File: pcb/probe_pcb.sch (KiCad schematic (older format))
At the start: 19 parts

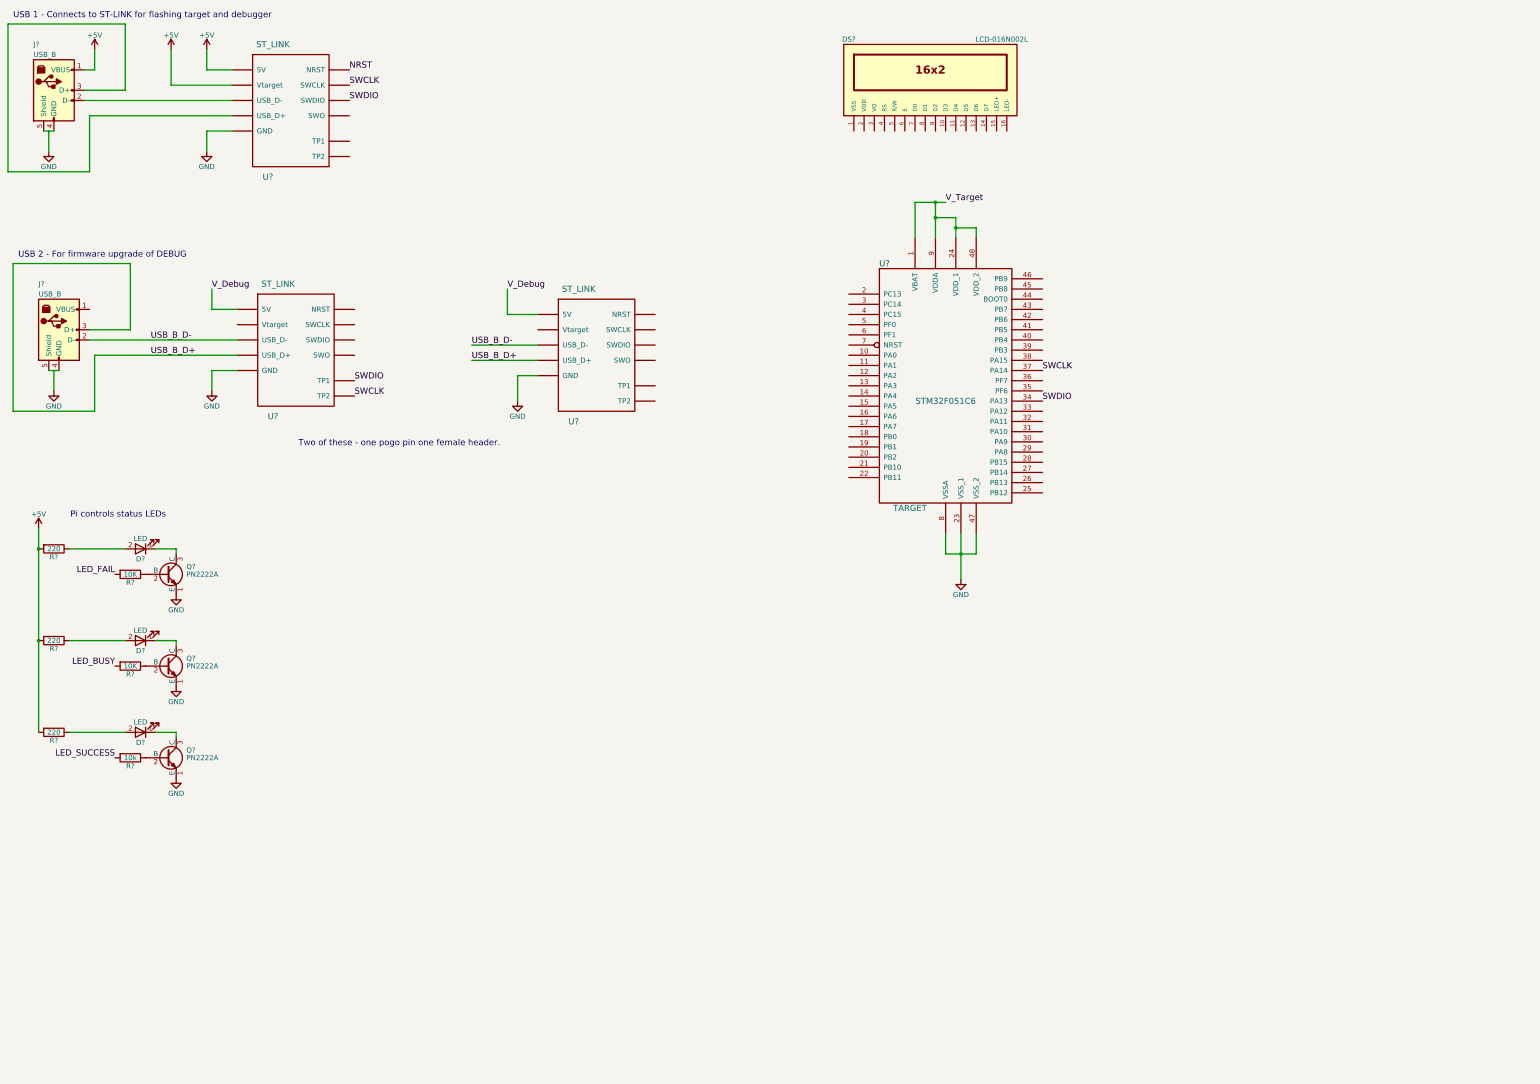
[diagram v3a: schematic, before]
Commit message: Added rough circuit for switching V_Target and V_Debug
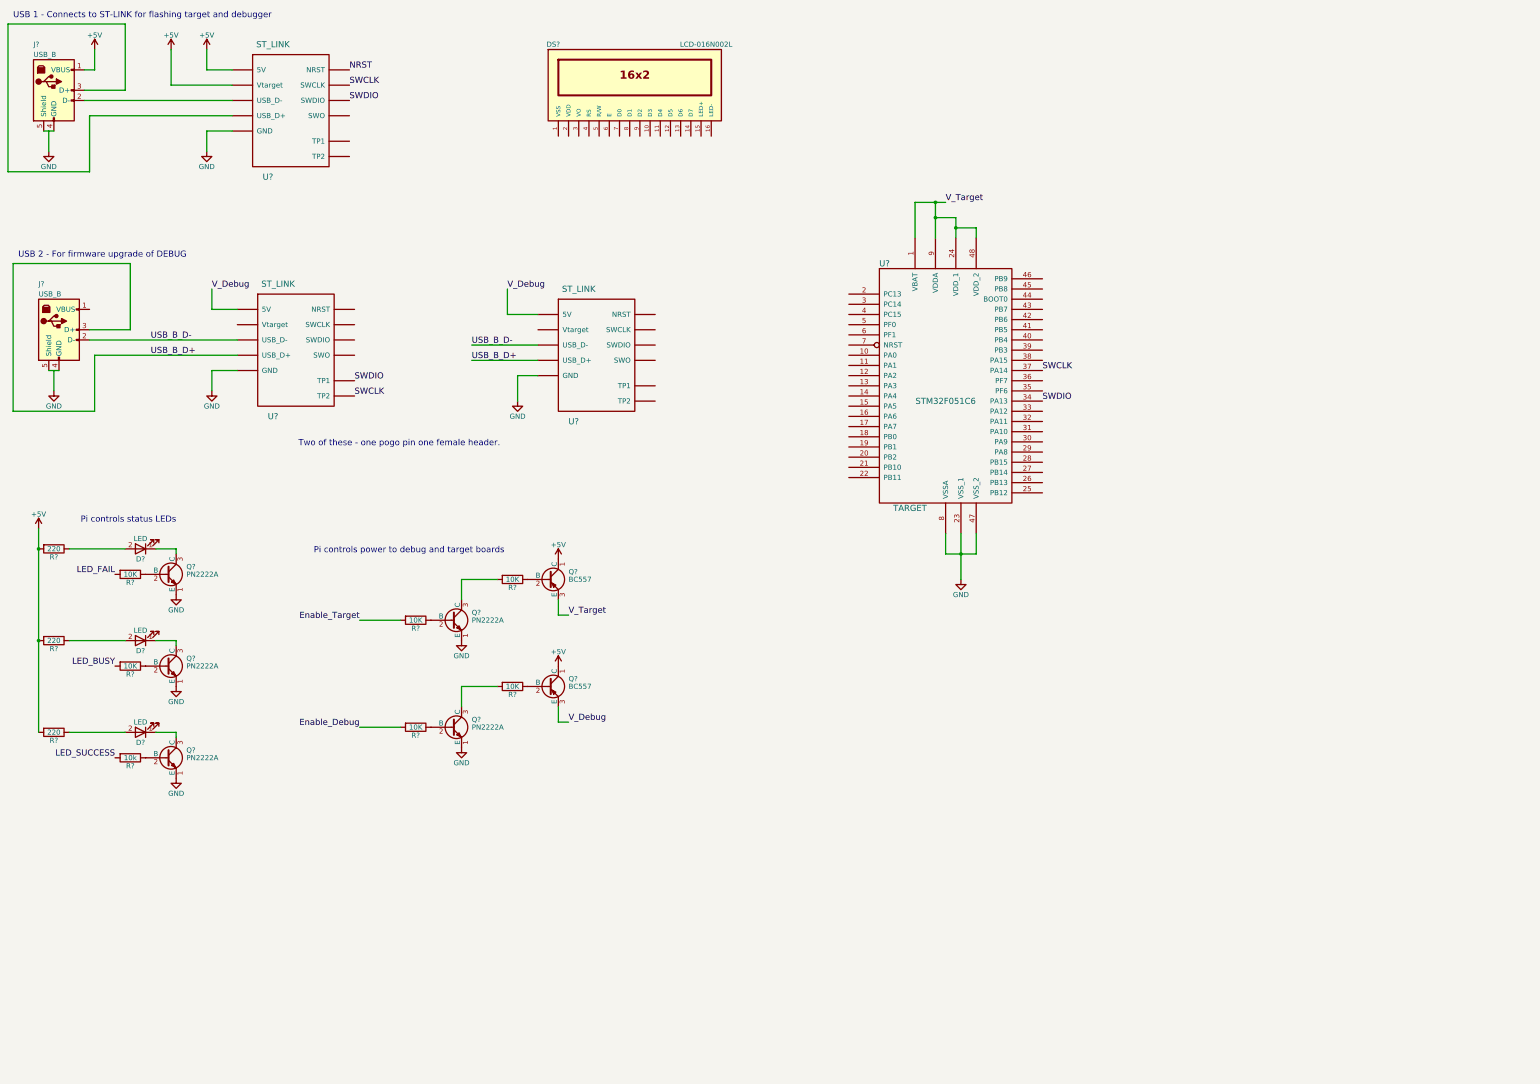
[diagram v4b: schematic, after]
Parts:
- added Q? (x2): PN2222A, TO_SOT_Packages_THT:TO-92_Molded_Narrow, symbol PN2222A
- added Q? (x2): BC557, TO_SOT_Packages_THT:TO-92_Molded_Narrow, symbol BC557
- added R? (x4): 10K, symbol R
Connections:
- net labels added: Enable_Debug, Enable_Target
- wire segments 59 -> 69
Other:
- note added: "Pi controls power to debug and target boards"
- moved on the sheet: DS?
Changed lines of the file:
@@
 L LCD-016N002L DS?
 U 1 1 5975A4A1
-P 9750 1300
-F 0 "DS?" H 8950 1700 50  0000 C CNN
-F 1 "LCD-016N002L" H 10450 1700 50  0000 C CNN
-F 2 "WC1602A" H 9750 1250 50  0001 C CIN
-F 3 "" H 9750 1300 50  0001 C CNN
-	1    9750 1300
+P 6850 1350
+F 0 "DS?" H 6050 1750 50  0000 C CNN
+F 1 "LCD-016N002L" H 7550 1750 50  0000 C CNN
+F 2 "WC1602A" H 6850 1300 50  0001 C CIN
+F 3 "" H 6850 1350 50  0001 C CNN
+	1    6850 1350
 	1    0    0    -1
 $EndComp
@@
 	0    1    1    0
 $EndComp
-Text Notes 2250 5600 2    60   ~ 0
+Text Notes 2350 5650 2    60   ~ 0
 Pi controls status LEDs
+Text Label 4150 6600 2    60   ~ 0
+Enable_Target
+$Comp
+L PN2222A Q?
+U 1 1 5975FD73
+P 5050 6600
+F 0 "Q?" H 5250 6675 50  0000 L CNN
+F 1 "PN2222A" H 5250 6600 50  0000 L CNN
+F 2 "TO_SOT_Packages_THT:TO-92_Molded_Narrow" H 5250 6525 50  0001 L CIN
+F 3 "" H 5050 6600 50  0001 L CNN
+	1    5050 6600
+	1    0    0    -1
+$EndComp
+$Comp
+L R R?
+U 1 1 5975FDE6
+P 4700 6600
+F 0 "R?" V 4780 6600 50  0000 C CNN
+F 1 "10K" V 4700 6600 50  0000 C CNN
+F 2 "" V 4630 6600 50  0001 C CNN
+F 3 "" H 4700 6600 50  0001 C CNN
+	1    4700 6600
+	0    1    1    0
+$EndComp
+Wire Wire Line
+	4550 6600 4150 6600
+$Comp
+L GND #PWR?
+U 1 1 5975FEEC
+P 5150 6800
+F 0 "#PWR?" H 5150 6550 50  0001 C CNN
+F 1 "GND" H 5150 6650 50  0000 C CNN
+F 2 "" H 5150 6800 50  0001 C CNN
+F 3 "" H 5150 6800 50  0001 C CNN
+	1    5150 6800
+	1    0    0    -1
+$EndComp
+$Comp
+L R R?
+U 1 1 5975FF2A
+P 5650 6200
+F 0 "R?" V 5730 6200 50  0000 C CNN
+F 1 "10K" V 5650 6200 50  0000 C CNN
+F 2 "" V 5580 6200 50  0001 C CNN
+F 3 "" H 5650 6200 50  0001 C CNN
+	1    5650 6200
+	0    1    1    0
+$EndComp
+Wire Wire Line
+	5150 6400 5150 6200
+Wire Wire Line
+	5150 6200 5500 6200
+$Comp
+L BC557 Q?
+U 1 1 5976007D
+P 6000 6200
+F 0 "Q?" H 6200 6275 50  0000 L CNN
+F 1 "BC557" H 6200 6200 50  0000 L CNN
+F 2 "TO_SOT_Packages_THT:TO-92_Molded_Narrow" H 6200 6125 50  0001 L CIN
+F 3 "" H 6000 6200 50  0001 L CNN
+	1    6000 6200
+	1    0    0    -1
+$EndComp
+$Comp
+L +5V #PWR?
+U 1 1 597600C6
+P 6100 6000
+F 0 "#PWR?" H 6100 5850 50  0001 C CNN
+F 1 "+5V" H 6100 6140 50  0000 C CNN
+F 2 "" H 6100 6000 50  0001 C CNN
+F 3 "" H 6100 6000 50  0001 C CNN
+	1    6100 6000
+	1    0    0    -1
+$EndComp
+Wire Wire Line
+	6100 6400 6100 6550
+Wire Wire Line
+	6100 6550 6200 6550
+Text Label 6200 6550 0    60   ~ 0
+V_Target
+Text Label 4150 7650 2    60   ~ 0
+Enable_Debug
+$Comp
+L PN2222A Q?
+U 1 1 59760565
+P 5050 7650
+F 0 "Q?" H 5250 7725 50  0000 L CNN
+F 1 "PN2222A" H 5250 7650 50  0000 L CNN
+F 2 "TO_SOT_Packages_THT:TO-92_Molded_Narrow" H 5250 7575 50  0001 L CIN
+F 3 "" H 5050 7650 50  0001 L CNN
+	1    5050 7650
+	1    0    0    -1
+$EndComp
+$Comp
+L R R?
+U 1 1 5976056B
+P 4700 7650
+F 0 "R?" V 4780 7650 50  0000 C CNN
+F 1 "10K" V 4700 7650 50  0000 C CNN
+F 2 "" V 4630 7650 50  0001 C CNN
+F 3 "" H 4700 7650 50  0001 C CNN
+	1    4700 7650
+	0    1    1    0
+$EndComp
+Wire Wire Line
+	4550 7650 4150 7650
+$Comp
+L GND #PWR?
+U 1 1 59760572
+P 5150 7850
+F 0 "#PWR?" H 5150 7600 50  0001 C CNN
+F 1 "GND" H 5150 7700 50  0000 C CNN
+F 2 "" H 5150 7850 50  0001 C CNN
+F 3 "" H 5150 7850 50  0001 C CNN
+	1    5150 7850
+	1    0    0    -1
+$EndComp
+$Comp
+L R R?
+U 1 1 59760578
+P 5650 7250
+F 0 "R?" V 5730 7250 50  0000 C CNN
+F 1 "10K" V 5650 7250 50  0000 C CNN
+F 2 "" V 5580 7250 50  0001 C CNN
+F 3 "" H 5650 7250 50  0001 C CNN
+	1    5650 7250
+	0    1    1    0
+$EndComp
+Wire Wire Line
+	5150 7450 5150 7250
+Wire Wire Line
+	5150 7250 5500 7250
+$Comp
+L BC557 Q?
+U 1 1 59760580
+P 6000 7250
+F 0 "Q?" H 6200 7325 50  0000 L CNN
+F 1 "BC557" H 6200 7250 50  0000 L CNN
+F 2 "TO_SOT_Packages_THT:TO-92_Molded_Narrow" H 6200 7175 50  0001 L CIN
+F 3 "" H 6000 7250 50  0001 L CNN
+	1    6000 7250
+	1    0    0    -1
+$EndComp
+$Comp
+L +5V #PWR?
+U 1 1 59760586
+P 6100 7050
+F 0 "#PWR?" H 6100 6900 50  0001 C CNN
+F 1 "+5V" H 6100 7190 50  0000 C CNN
+F 2 "" H 6100 7050 50  0001 C CNN
+F 3 "" H 6100 7050 50  0001 C CNN
+	1    6100 7050
+	1    0    0    -1
+$EndComp
+Wire Wire Line
+	6100 7450 6100 7600
+Wire Wire Line
+	6100 7600 6200 7600
+Text Label 6200 7600 0    60   ~ 0
+V_Debug
+Text Notes 3700 5950 0    60   ~ 0
+Pi controls power to debug and target boards
 $EndSCHEMATC

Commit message: Started on LCD, replaced transistors
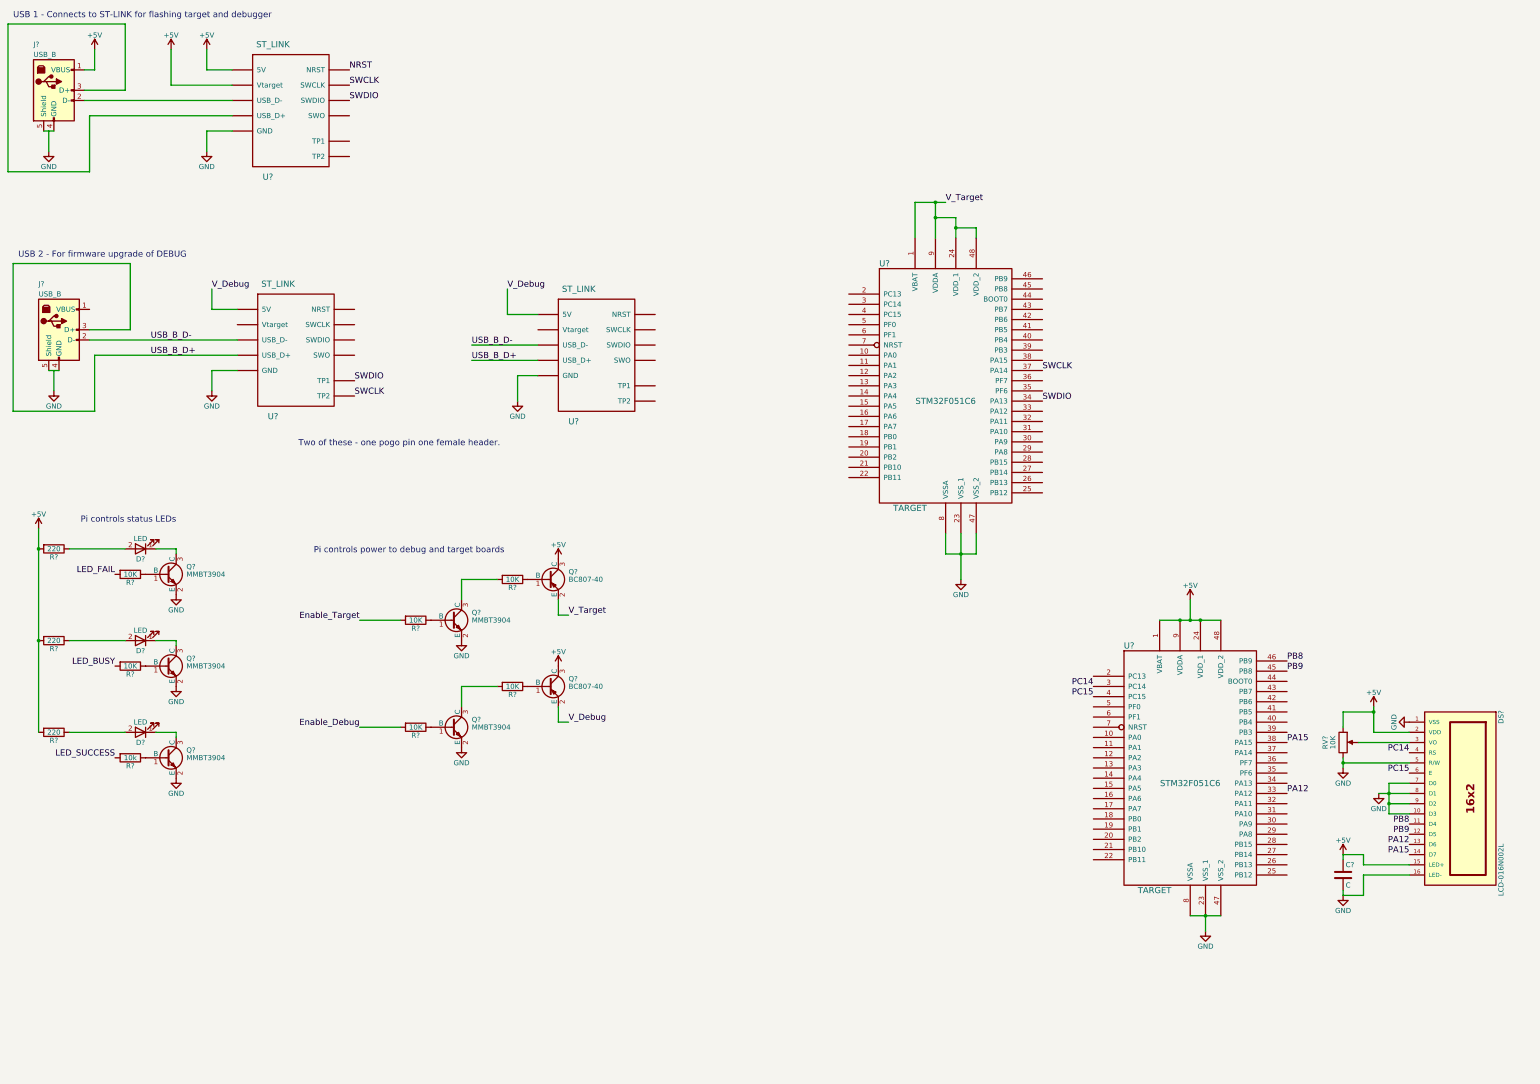
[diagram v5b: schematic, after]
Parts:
- removed Q? (x5): PN2222A, TO_SOT_Packages_THT:TO-92_Molded_Narrow, symbol PN2222A
- removed Q? (x2): BC557, TO_SOT_Packages_THT:TO-92_Molded_Narrow, symbol BC557
- added C?: C, symbol C
- added Q? (x5): MMBT3904, TO_SOT_Packages_SMD:SOT-23, symbol MMBT3904
- added Q? (x2): BC807-40, TO_SOT_Packages_SMD:SOT-23, symbol BC807-40
- added RV?: 10K, symbol POT
- added U?: TARGET, STM32F051C6, symbol TARGET
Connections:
- net +5V: now also DS?.15 (LED+), DS?.2 (VDD), C?.1, Q?.3 (C), Q?.3 (C), RV?.1, U?.1 (VBAT), U?.24 (VDD_1), U?.48 (VDD_2), U?.9 (VDDA)
- net GND: now also DS?.1 (VSS), DS?.10 (D3), DS?.16 (LED-), DS?.5 (R/W), DS?.7 (D0), DS?.8 (D1), DS?.9 (D2), C?.2, Q?.2 (E), Q?.2 (E), Q?.2 (E), Q?.2 (E), Q?.2 (E), RV?.3, U?.23 (VSS_1), U?.47 (VSS_2), U?.8 (VSSA)
- net V_Debug: now also Q?.2 (E)
- net V_Target: now also Q?.2 (E)
- net PB8: now reaches DS?.11 (D4)
- net PB8: now also U?.46 (PB9)
- net PB9: now reaches DS?.12 (D5)
- net PB9: now also U?.45 (PB8)
- net PA12: now reaches DS?.13 (D6)
- net PA12: now also U?.33 (PA12)
- net PA15: now reaches DS?.14 (D7)
- net PA15: now also U?.38 (PA15)
- net at DS?.3 (VO): now also RV?.2
- net PC14: now reaches DS?.4 (RS)
- net PC14: now also U?.3 (PC14)
- net PC15: now reaches DS?.6 (E)
- net PC15: now also U?.4 (PC15)
- net at D?.1 (K): now also Q?.3 (C) (x3)
- net at R?.1: now also Q?.1 (B) (x7)
- net at R?.2: now also Q?.3 (C) (x2)
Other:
- moved on the sheet: DS?

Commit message: Finished LCD, added target and debug buttons, as well as some extra status LEDs
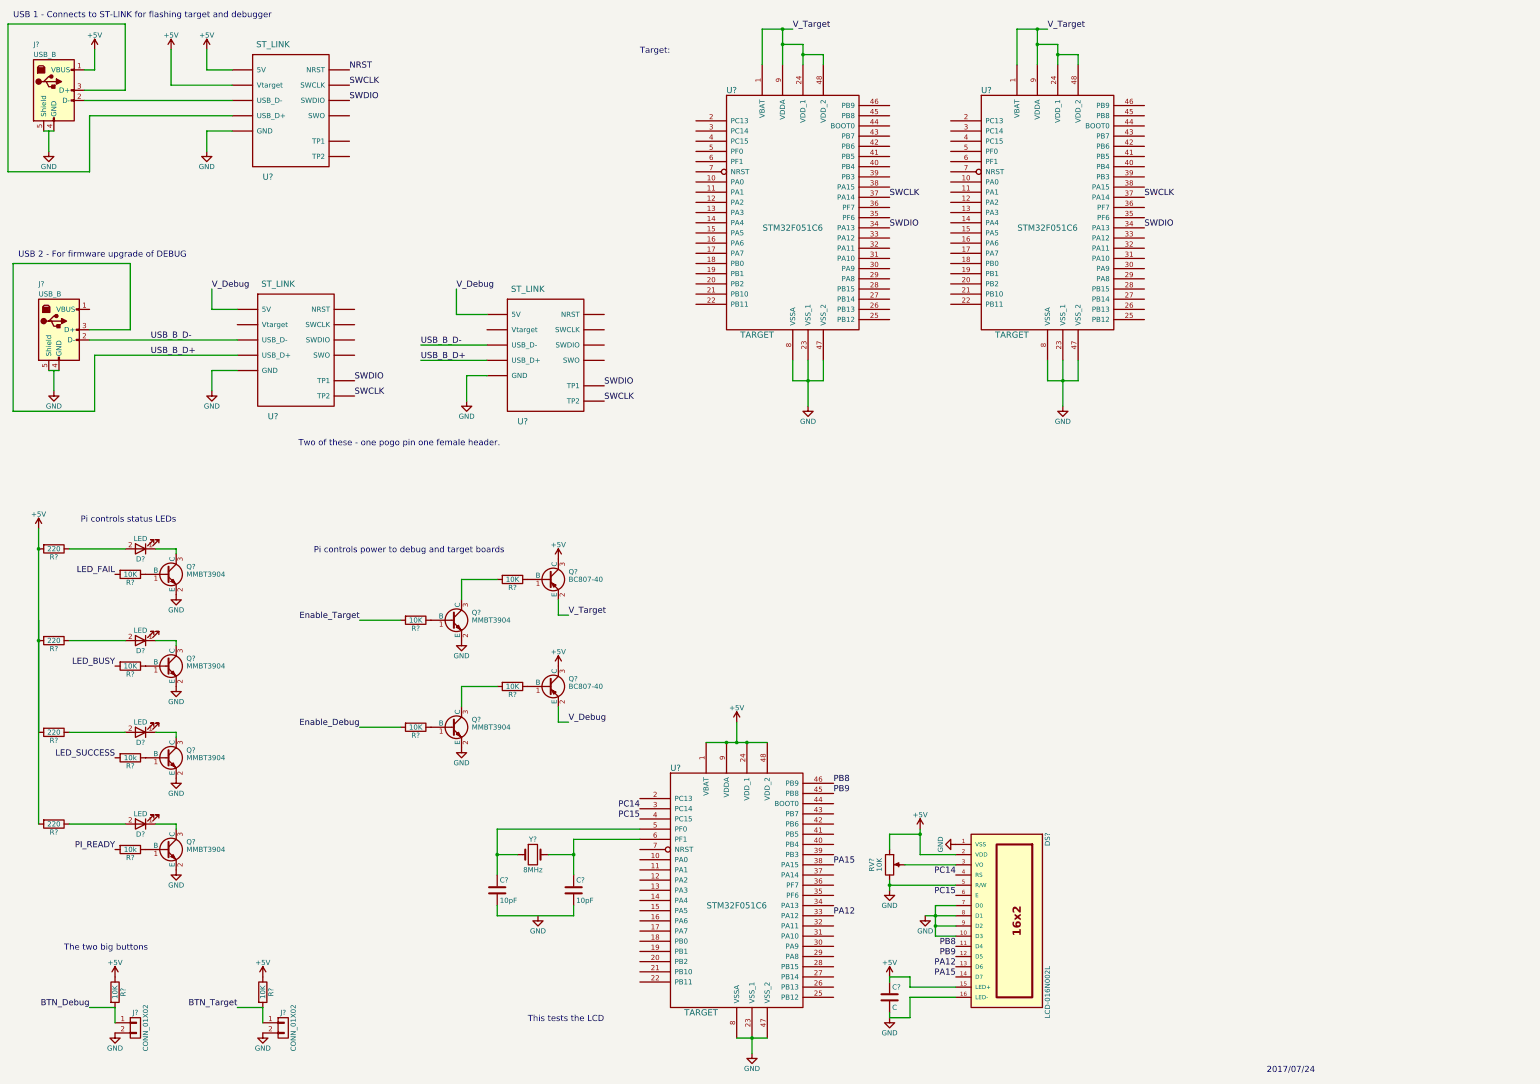
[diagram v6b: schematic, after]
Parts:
- added C? (x2): 10pF, symbol C
- added D?: LED, symbol LED
- added J? (x2): CONN_01X02, symbol CONN_01X02
- added Q?: MMBT3904, TO_SOT_Packages_SMD:SOT-23, symbol MMBT3904
- added R?: 220, symbol R
- added R?: 10k, symbol R
- added R? (x2): 10K, symbol R
- added U?: TARGET, STM32F051C6, symbol TARGET
- added Y?: 8MHz, symbol Crystal
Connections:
- net +5V: now also R?.1, R?.1, R?.2
- net GND: now also J?.2 (P2), J?.2 (P2), Q?.2 (E), U?.23 (VSS_1), U?.47 (VSS_2), U?.8 (VSSA)
- net SWCLK: now also U?.~ (Vtarget), U?.37 (PA14)
- net SWDIO: now also U?.~ (Vtarget), U?.34 (PA13)
- net V_Target: now also U?.1 (VBAT), U?.24 (VDD_1), U?.48 (VDD_2), U?.9 (VDDA)
- net at U?.5 (PF0): now also C?.1, Y?.1
- net at U?.6 (PF1): now also C?.1, Y?.2
- new net: C?.2, C?.2
- new net: D?.1 (K), Q?.3 (C)
- new net: D?.2 (A), R?.1
- new net: Q?.1 (B), R?.1
- new net BTN_Debug: J?.1 (P1), R?.2
- new net BTN_Target: J?.1 (P1), R?.2
- new net PI_READY: R?.2
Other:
- note added: "2017/07/24"
- note added: "Target:"
- note added: "The two big buttons"
- note added: "This tests the LCD"
- moved on the sheet: C?, DS?, RV?, U?
